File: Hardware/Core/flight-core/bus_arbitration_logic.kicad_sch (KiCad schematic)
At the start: 14 parts, among them U10 SN74LVC2G04DBVR, U11 SN74LV32APWR, U12 SN74LVC2G08DCUT, U8 SN74LVC2G07DBVR, U9 SN74LVC2G132DCTR

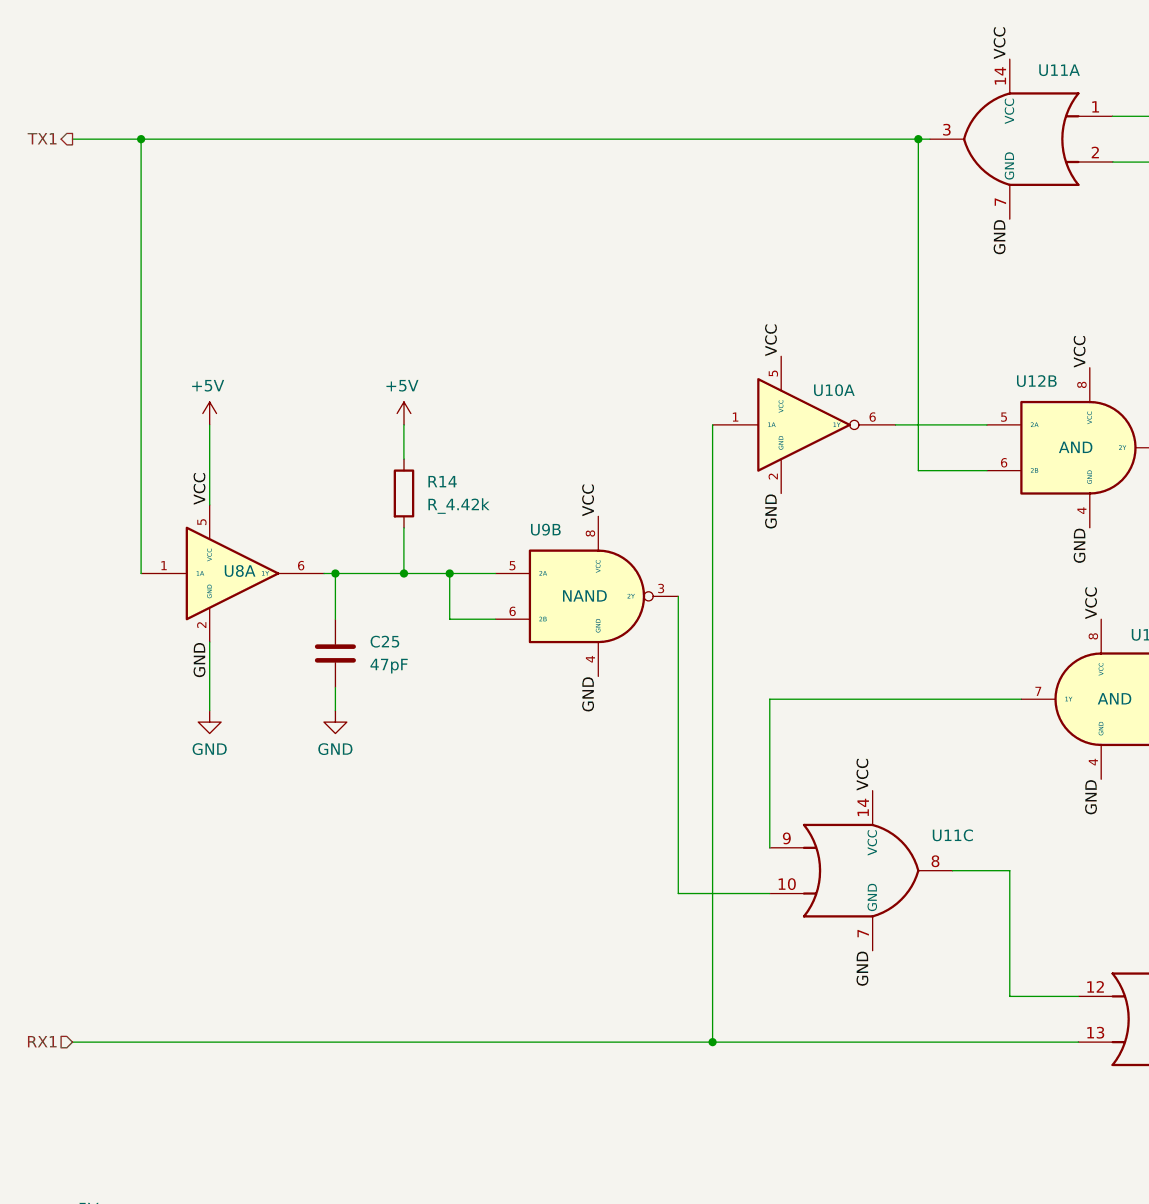
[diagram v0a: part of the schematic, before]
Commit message: swapped 5 & 6 in bus arb, placed components
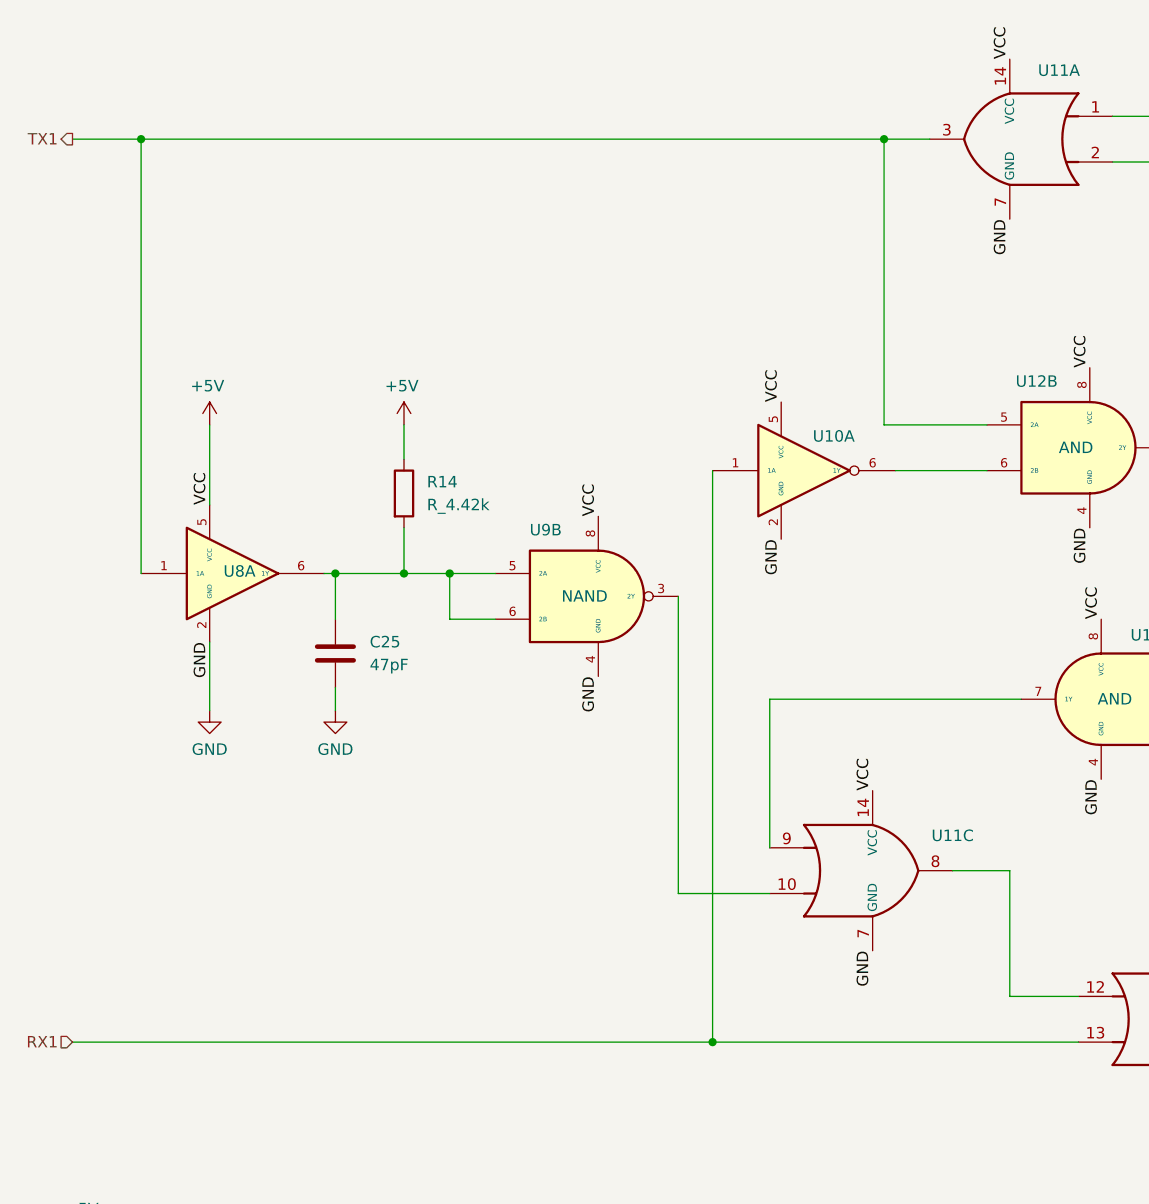
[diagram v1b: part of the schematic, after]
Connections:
- net TX1: now also U12.5 (2A); no longer U12.6 (2B)
- net at U10.6 (1Y): now also U12.6 (2B); no longer U12.5 (2A)
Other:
- moved on the sheet: U10A
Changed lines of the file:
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@@
+	)
+	(junction
+		(at 127 31.75)
+		(diameter 0)
+		(color 0 0 0 0)
 	)
 	(junction
@@
 	)
 	(junction
-		(at 130.81 31.75)
-		(diameter 0)
-		(color 0 0 0 0)
-	)
-	(junction
 		(at 50.8 166.37)
 		(diameter 0)
@@
 	(wire
 		(pts
+			(xy 138.43 63.5) (xy 127 63.5)
+		)
+		(stroke
+			(width 0)
+			(type default)
+		)
+	)
+	(wire
+		(pts
 			(xy 215.9 80.01) (xy 220.98 80.01)
 		)
@@
 	(wire
 		(pts
-			(xy 130.81 68.58) (xy 138.43 68.58)
-		)
-		(stroke
-			(width 0)
-			(type default)
-		)
-	)
-	(wire
-		(pts
 			(xy 78.74 80.01) (xy 78.74 85.09)
 		)
@@
 	(wire
 		(pts
-			(xy 107.95 63.5) (xy 107.95 132.08)
+			(xy 107.95 68.58) (xy 107.95 132.08)
 		)
 		(stroke
@@
 	(wire
 		(pts
-			(xy 44.45 31.75) (xy 130.81 31.75)
+			(xy 44.45 31.75) (xy 127 31.75)
 		)
 		(stroke
@@
 	(wire
 		(pts
-			(xy 130.81 31.75) (xy 130.81 68.58)
-		)
-		(stroke
-			(width 0)
-			(type default)
-		)
-	)
-	(wire
-		(pts
 			(xy 158.75 66.04) (xy 180.34 66.04)
 		)
@@
 	(wire
 		(pts
-			(xy 128.27 63.5) (xy 138.43 63.5)
-		)
-		(stroke
-			(width 0)
-			(type default)
-		)
-	)
-	(wire
-		(pts
 			(xy 114.3 93.98) (xy 114.3 110.49)
 		)
@@
 	(wire
 		(pts
-			(xy 130.81 31.75) (xy 132.08 31.75)
-		)
-		(stroke
-			(width 0)
-			(type default)
-		)
-	)
-	(wire
-		(pts
 			(xy 157.48 34.29) (xy 157.48 48.26)
 		)
@@
 	(wire
 		(pts
+			(xy 127 31.75) (xy 132.08 31.75)
+		)
+		(stroke
+			(width 0)
+			(type default)
+		)
+	)
+	(wire
+		(pts
 			(xy 152.4 29.21) (xy 189.23 29.21)
 		)
@@
 	(wire
 		(pts
+			(xy 128.27 68.58) (xy 138.43 68.58)
+		)
+		(stroke
+			(width 0)
+			(type default)
+		)
+	)
+	(wire
+		(pts
 			(xy 189.23 29.21) (xy 266.7 29.21)
 		)
@@
 		(pts
 			(xy 168.91 129.54) (xy 171.45 129.54)
+		)
+		(stroke
+			(width 0)
+			(type default)
+		)
+	)
+	(wire
+		(pts
+			(xy 127 63.5) (xy 127 31.75)
 		)
 		(stroke
@@
 	)
 	(label "GND"
-		(at 115.57 71.12 270)
+		(at 115.57 76.2 270)
 		(effects
 			(font
@@
 	)
 	(label "VCC"
-		(at 115.57 55.88 90)
+		(at 115.57 60.96 90)
 		(effects
 			(font
@@
 	(symbol
 		(lib_id "OlinBAD:SN74LVC2G04DBVR_2U_Inverter")
-		(at 115.57 63.5 0)
+		(at 115.57 68.58 0)
 		(unit 1)
 		(exclude_from_sim no)
@@
 		(dnp no)
 		(property "Reference" "U10"
-			(at 121.412 59.69 0)
+			(at 121.412 64.77 0)
 			(effects
 				(font
@@
 		)
 		(property "Value" "SN74LVC2G04DBVR"
-			(at 102.87 59.9692 0)
+			(at 102.87 65.0492 0)
 			(effects
 				(font
@@
 		)
 		(property "Footprint" "obad_footprints:SOT95P280X145-6N"
-			(at 115.57 63.5 0)
+			(at 115.57 68.58 0)
 			(effects
 				(font
@@
 		)
 		(property "Datasheet" "https://www.ti.com/lit/ds/symlink/sn74lvc2g04.pdf?HQS=dis-dk-null-digikeymode-dsf-pf-null-wwe&ts=1761945422821&ref_url=https%253A%252F%252Fwww.ti.com%252Fgeneral%252Fdocs%252Fsuppproductinfo.tsp%253FdistId%253D10%2526gotoUrl%253Dhttps%253A%252F%252Fwww.ti.com%252Flit%252Fgpn%252Fsn74lvc2g04"
-			(at 115.57 63.5 0)
+			(at 115.57 68.58 0)
 			(effects
 				(font
@@
 		)
 		(property "Description" "IC INVERTER 2CH 2-INP SOT23-6"
-			(at 115.57 63.5 0)
+			(at 115.57 68.58 0)
 			(effects
 				(font
@@
 		)
 		(property "Label" "Inverter"
-			(at 115.57 63.5 0)
-			(effects
-				(font
+			(at 115.57 68.58 0)
+			(effects
+				(font
